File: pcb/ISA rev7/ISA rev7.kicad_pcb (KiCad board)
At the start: 2 copper layers, 99.6 x 68.3 mm, 38 parts, among them J1 PCB_Finger_ISA_8bit, J2 Remote Connector, J3 Power Select Jumper, U1 74LVC02, U2 74LVC11, U3 74LVC245, U4 74LVC245, U5 74LVC245, U6 Pico

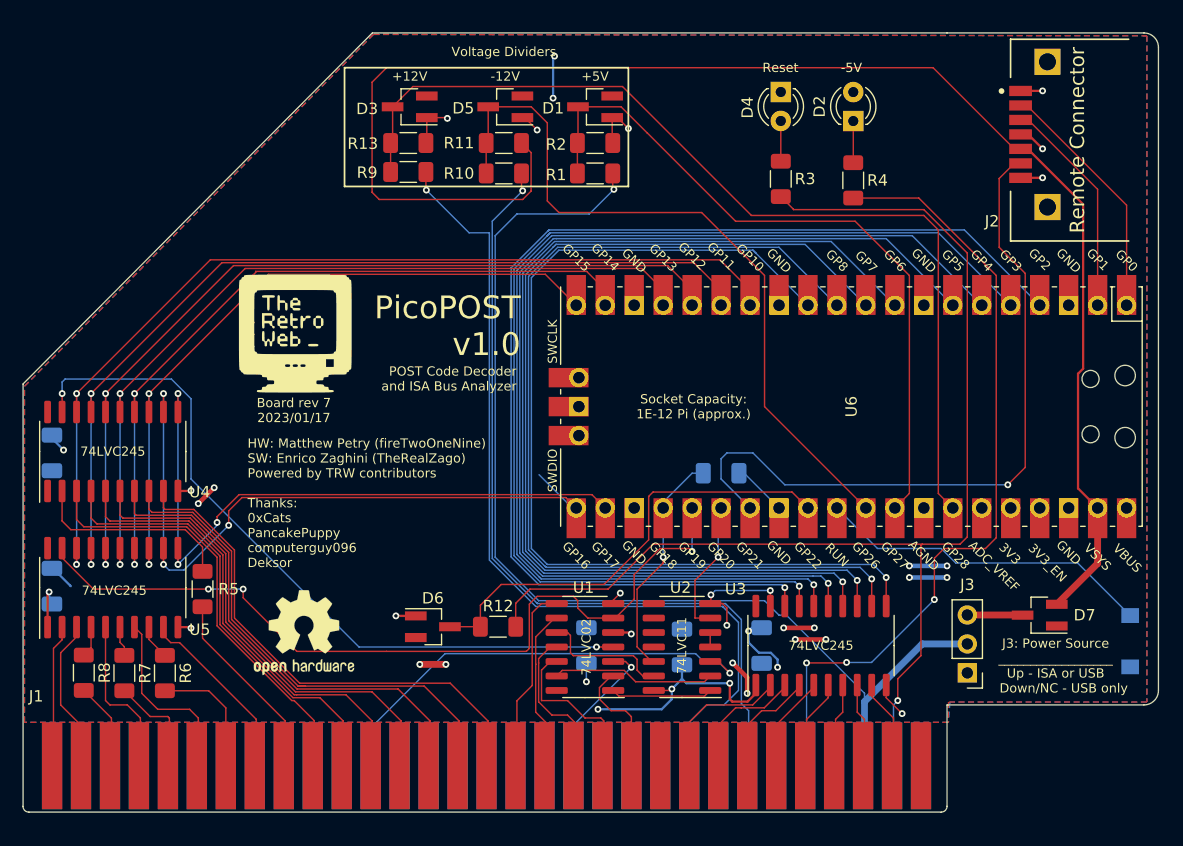
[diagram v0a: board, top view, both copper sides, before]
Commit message: Finalized rev7 including gerbers
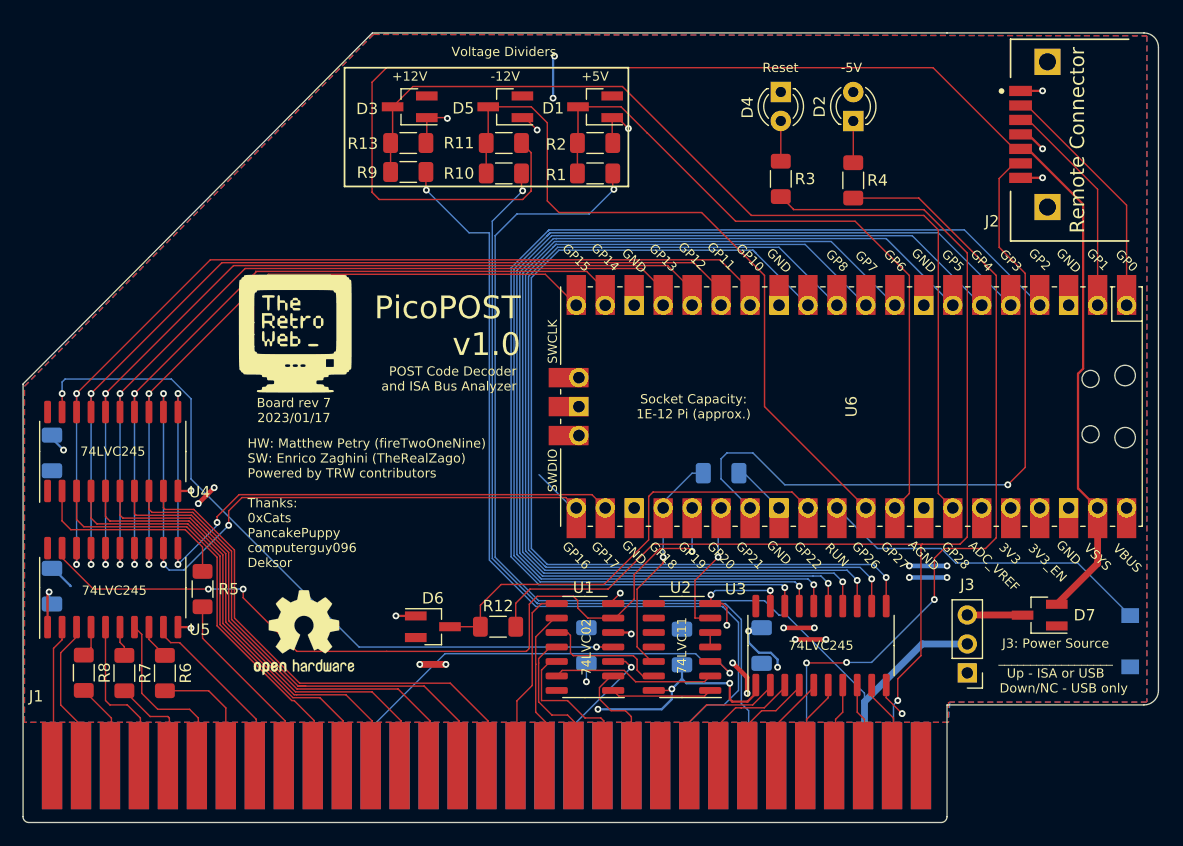
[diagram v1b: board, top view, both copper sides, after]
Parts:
- added .: LOGO, modified ICs:picopost_logo, B.Cu at (126.2, 78.2)
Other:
- board size 99.6 x 68.3 mm -> 99.6 x 69.2 mm
